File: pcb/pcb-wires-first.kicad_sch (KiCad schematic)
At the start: 61 parts, among them J1 Conn_01x04, J2 Conn_01x04, J3 Conn_01x04, J4 Conn_01x02, J5 Conn_01x02, J6 Conn_01x02, J7 Conn_01x02, J8 Conn_01x04, SW1 on-1, SW2 off-1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

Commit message: Completely reworking the entire thing. It is sinble-channel now.
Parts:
- removed C1, C10, C11, C12, C13, C2, C3, C4, C5, C6, C7, C8, C9: 100nF, Capacitor_SMD:C_0603_1608Metric, symbol Device:C
- removed D1: ON1, Diode_SMD:D_0603_1608Metric, symbol Device:LED
- removed J1, J2, J3: Conn_01x04, Connector_Phoenix_MC:PhoenixContact_MCV_1,5_4-G-3.5_1x04_P3.50mm_Vertical, symbol Connector_Generic:Conn_01x04
- removed J6, J7: Conn_01x02, Connector_JST:JST_VH_B2P-VH_1x02_P3.96mm_Vertical, symbol Connector_Generic:Conn_01x02
- removed R1: 2.2k, Resistor_SMD:R_0603_1608Metric, symbol Device:R
- removed SW1: on-1, Button_Switch_SMD:SW_SPST_B3U-1000P, symbol Switch:SW_Push
- removed SW2: off-1, Button_Switch_SMD:SW_SPST_B3U-1000P, symbol Switch:SW_Push
- removed SW3: on-2, Button_Switch_SMD:SW_SPST_B3U-1000P, symbol Switch:SW_Push
- removed SW4: off-2, Button_Switch_SMD:SW_SPST_B3U-1000P, symbol Switch:SW_Push
- removed SW5: on-3, Button_Switch_SMD:SW_SPST_B3U-1000P, symbol Switch:SW_Push
- removed SW6: off-3, Button_Switch_SMD:SW_SPST_B3U-1000P, symbol Switch:SW_Push
- removed TP2: sw1, TestPoint:TestPoint_Keystone_5010-5014_Multipurpose, symbol Connector:TestPoint
- removed TP3: sw2, TestPoint:TestPoint_Keystone_5010-5014_Multipurpose, symbol Connector:TestPoint
- removed TP4: sw3, TestPoint:TestPoint_Keystone_5010-5014_Multipurpose, symbol Connector:TestPoint
- removed U1: SLG46826V, Package_DFN_QFN:Renesas_UQFN-20_2x3mm_P0.4mm_LayoutBorder4x6y, symbol local-lib:SLG46826V
- added C19, C20, C22: 100nF, Capacitor_SMD:C_0603_1608Metric, symbol Device:C
- added J6: Conn_01x04, Connector_Phoenix_MC:PhoenixContact_MCV_1,5_4-G-3.5_1x04_P3.50mm_Vertical, symbol Connector_Generic:Conn_01x04
- added NT2, NT3, NT4: NetTie_2, NetTie:NetTie-2_SMD_Pad0.5mm, symbol Device:NetTie_2
- added NT5: NetTie_2, NetTie:NetTie-2_THT_Pad0.3mm, symbol Device:NetTie_2
- added SW7: set, Button_Switch_SMD:SW_SPST_B3U-1000P, symbol Switch:SW_Push
- added SW8: reset, Button_Switch_SMD:SW_SPST_B3U-1000P, symbol Switch:SW_Push
- added SW9: toggle, Button_Switch_SMD:SW_SPST_B3U-1000P, symbol Switch:SW_Push
- C16: value 100nF -> 1000nF
- D3: value ON3 -> Blinker
- NT1: footprint (none) -> NetTie:NetTie-2_SMD_Pad0.5mm
- R2: value 2.2k -> 6.7k
- U2: symbol local-lib:SLG47105V -> local-lib:SLG47115V
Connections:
- net output-1 is gone; now on net output: J5.2 (Pin_2), U2.7 (HV_GPO0)
- net output-2 is gone; now on net output: U2.8 (HV_GPO0)
- net output-3 is gone; now on net output: U2.9 (HV_GPO1)
- net GND: now also C19.1, C20.1, C22.1, J6.1 (Pin_1), SW7.1, SW8.1, SW9.1; no longer D2.1 (K), D6.1 (K)
- net HV-GND: now also NT3.1, NT5.1
- net HV-VDD: now also NT2.2; no longer R6.1
- net at D4.2 (A): now also R4.1; no longer R4.2
- net output: now reaches U2.10 (HV_GPO1)
- net output: now also NT4.2
- net at U2.20 (GPIO6): now also C19.2, J6.3 (Pin_3), SW7.2
- net at U2.3 (GPI): now also C22.2, J6.2 (Pin_2), SW8.2
- removed net fault: A1.22 (A3), R4.1, U2.19 (GPIO5)
- net off-1b: no longer names the net of A1.1 (D1/TX)
- net off-2b: no longer names the net of A1.6 (D3)
- net off-3b: no longer names the net of A1.8 (D5)
- net on-1b: no longer names the net of A1.2 (D0/RX)
- net on-2b: no longer names the net of A1.5 (D2)
- net on-3b: no longer names the net of A1.7 (D4)
- net switch-1: no longer names the net of A1.21 (A2)
- net switch-1: no longer U2.2 (GPIO0)
- removed net switch-2: A1.20 (A1), R2.1, U2.14 (GPIO1)
- net switch-3: no longer names the net of R3.1, U2.17 (GPIO4)
- net switch-3: no longer A1.19 (A0)
- new net: D6.1 (K), NT3.2
- new net: C20.2, J6.4 (Pin_4), SW9.2, U2.19 (GPIO5)
- new net: NT2.1, R6.1
- new net: NT4.1, R2.1
- new net: D2.1 (K), NT5.2
- new net: R4.2, U2.14 (GPIO1)
- no-connect marks 20 -> 17
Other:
- note added: "Issues. 1. Input connectors do not have GND. 2. IO6 and IO7 are GPO on 46826. 3. It is 47105, not 47115. 4. Add blinker LEDs to each SLG. 5. Bigger power cap next to SLG."
- note removed: "Debounce capacitors (all 100nF)"
- note removed: "Issues. 1. Input connectors do not have GND. 2. IO6 and IO7 are GPO on 46826. 3. It is 47105, not 47115. 4. Add blinker LEDs to each SLG."
- moved on the sheet: A1, C14, C15, C16, C17, C18, D2, D3, D4, D5, D6, J4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

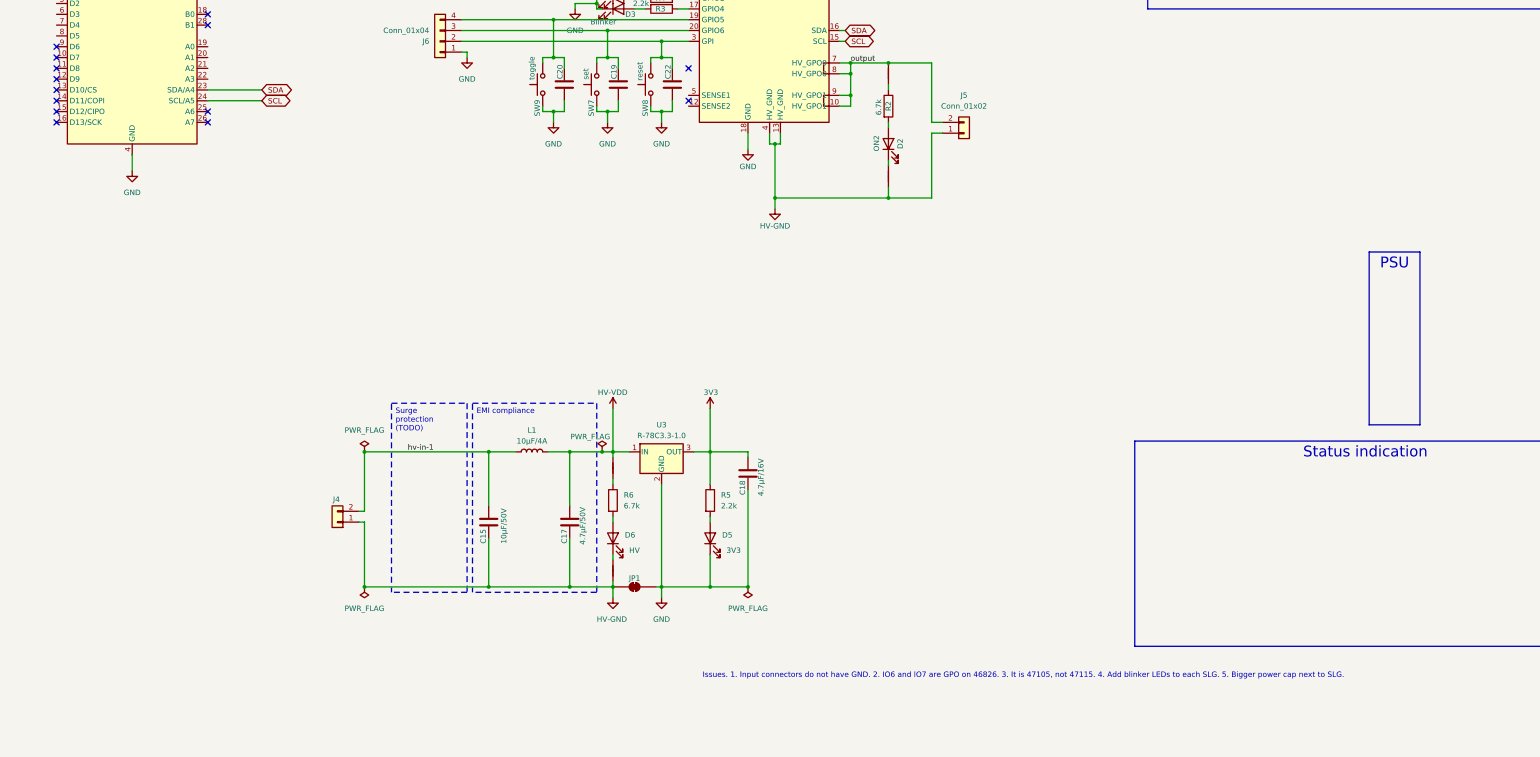
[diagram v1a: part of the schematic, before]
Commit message: Adding blinker for Arduino.
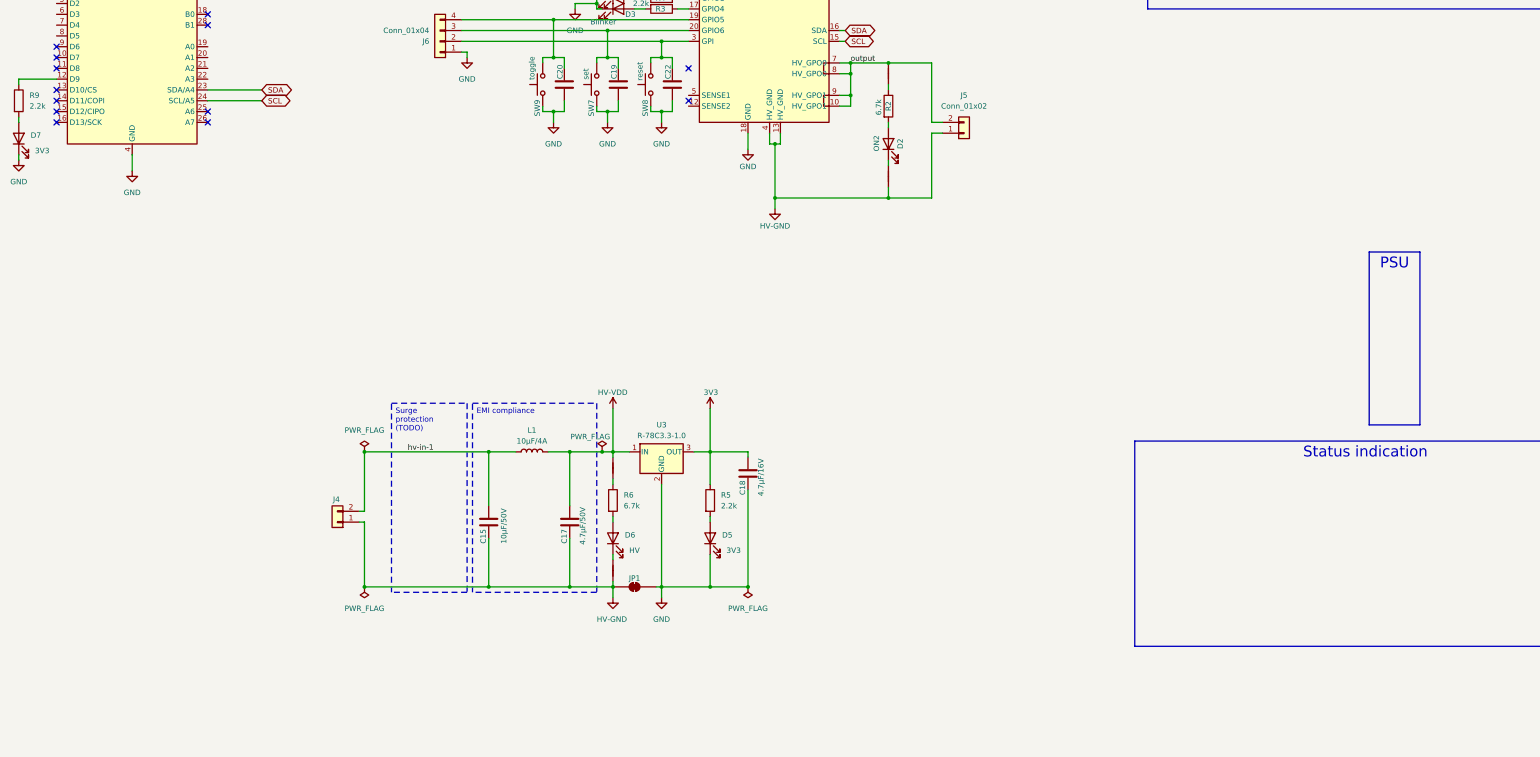
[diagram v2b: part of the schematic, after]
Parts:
- added D7: 3V3, Diode_SMD:D_0603_1608Metric, symbol Device:LED
- added R9: 2.2k, Resistor_SMD:R_0603_1608Metric, symbol Device:R
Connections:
- net GND: now also D7.1 (K)
- net at A1.12 (D9): now also R9.1
- new net: D7.2 (A), R9.2
- no-connect marks 17 -> 16
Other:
- note removed: "Issues. 1. Input connectors do not have GND. 2. IO6 and IO7 are GPO on 46826. 3. It is 47105, not 47115. 4. Add blinker LEDs to each SLG. 5. Bigger power cap next to SLG."

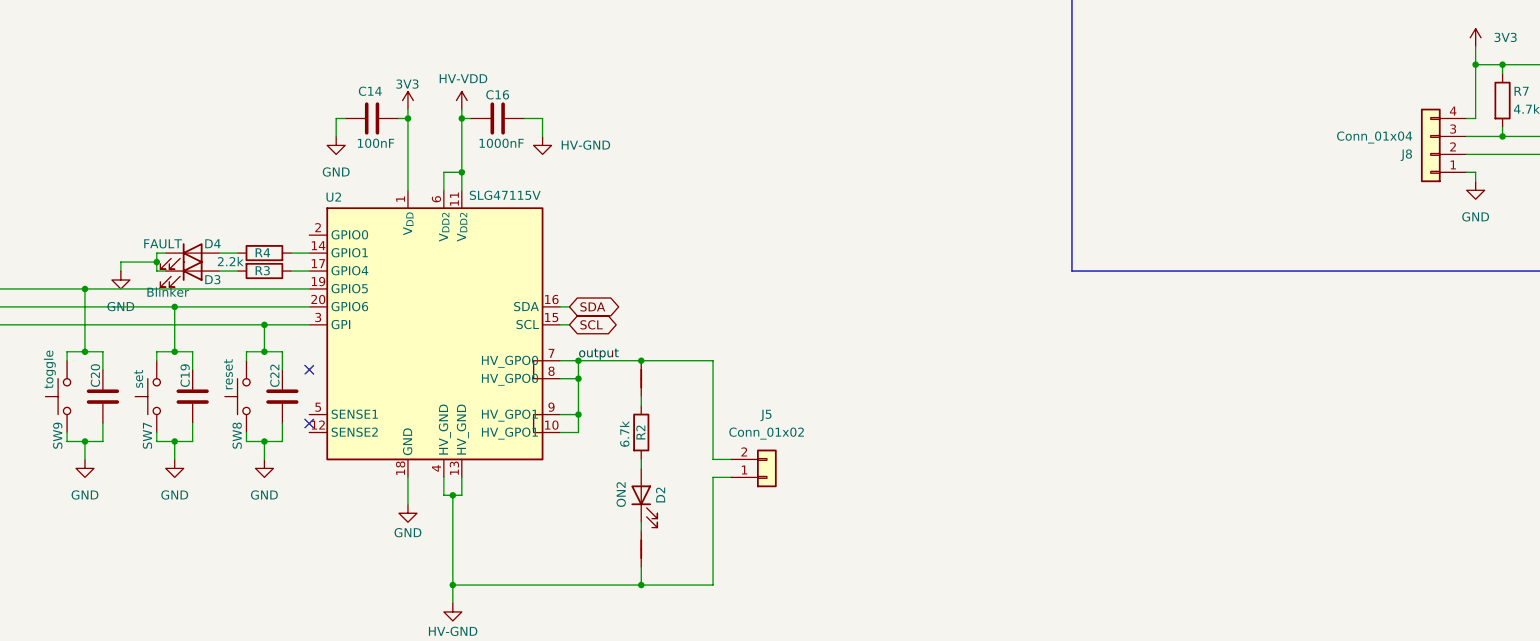
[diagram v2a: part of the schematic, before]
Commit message: Cleaning up DRC violations in PCB.
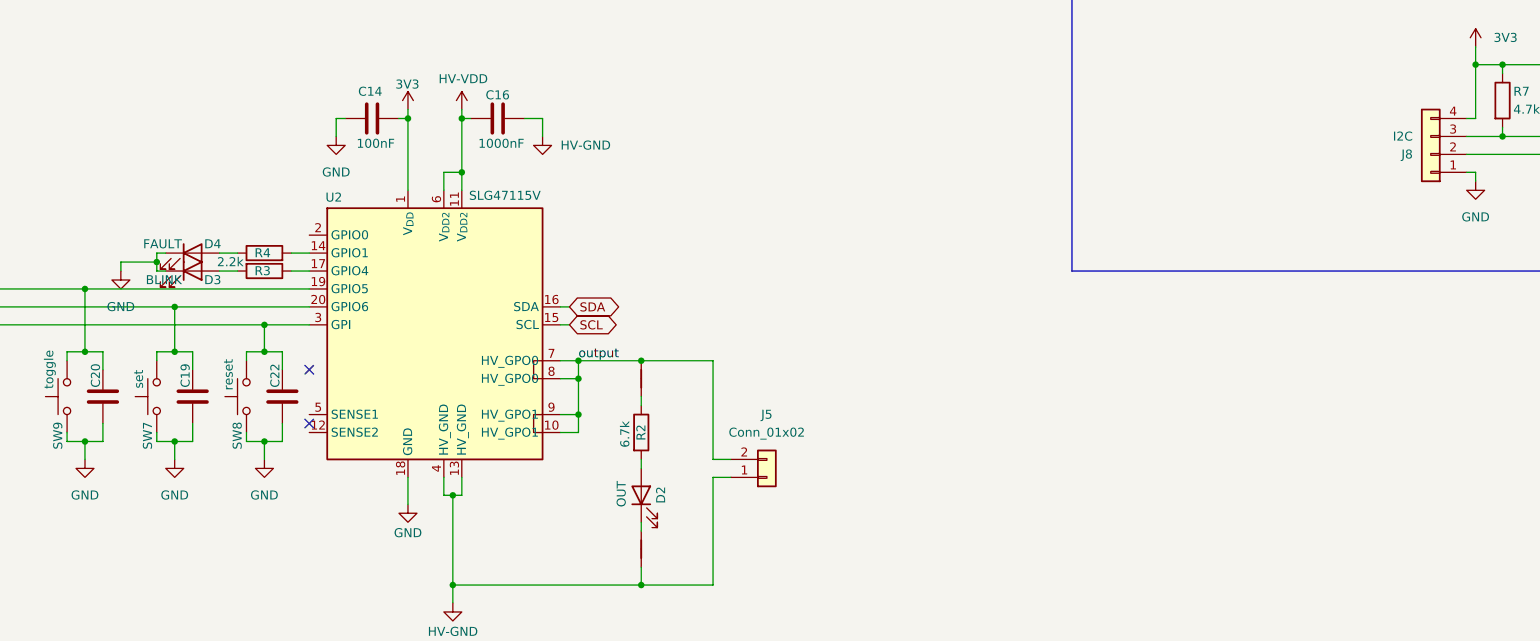
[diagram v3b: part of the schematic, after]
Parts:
- D2: value ON2 -> OUT
- D3: value Blinker -> BLINK
- J8: value Conn_01x04 -> I2C
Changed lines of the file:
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@@
 			)
 		)
-		(property "Value" "Conn_01x04"
+		(property "Value" "I2C"
 			(at 350.52 39.3701 0)
 			(show_name no)
@@
 			)
 		)
-		(property "Value" "Blinker"
-			(at 177.292 61.468 0)
+		(property "Value" "BLINK"
+			(at 176.276 59.69 0)
 			(show_name no)
 			(do_not_autoplace no)
@@
 			)
 		)
-		(property "Value" "ON2"
+		(property "Value" "OUT"
 			(at 238.506 88.138 0)
 			(show_name no)

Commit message: Some more cleanup.
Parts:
- D7: value 3V3 -> BLINK
- J5: value Conn_01x02 -> OUT
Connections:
- no-connect marks 16 -> 27
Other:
- note added: "Arduino"
- note added: "I2C"
- note added: "Misc"
- note added: "PSU"
- note added: "Power switcher"
- moved on the sheet: A1, C14, C15, C16, C17, C18, C19, C20, C22, D2, D3, D4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

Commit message: Updating to new libs.
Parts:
- H1, H2, H3, H4: footprint Local:MountingHole_3.2mm_M3 -> MountingHole:MountingHole_3.2mm_M3_NoCopper
- U2: symbol local-lib:SLG47115V -> CPLD_Renesas:SLG47115V
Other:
- moved on the sheet: C14, C16, C19, C20, C22, D3, D4, J6, R3, R4, SW7, SW8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
